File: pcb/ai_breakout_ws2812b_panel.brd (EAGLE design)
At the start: 92.2 x 100 mm, 280 parts

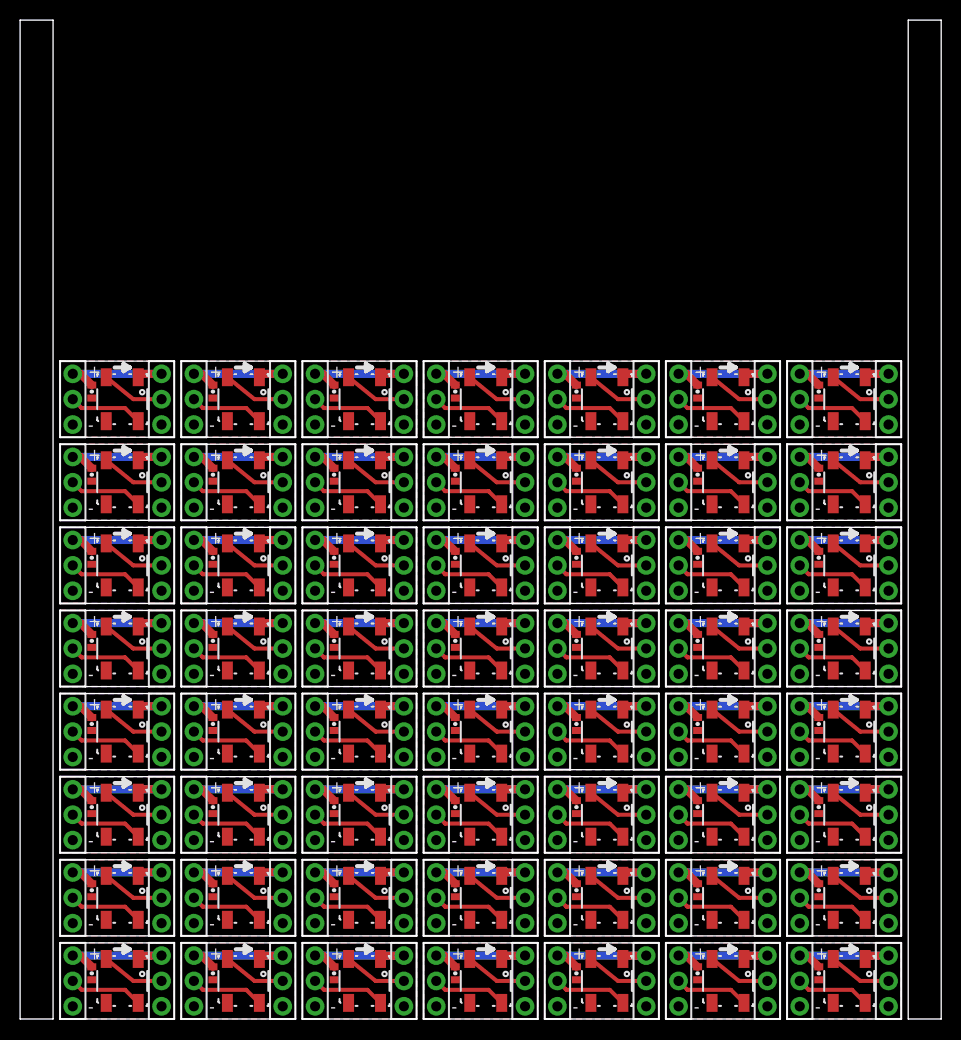
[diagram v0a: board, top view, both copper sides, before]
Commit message: adding panelized version
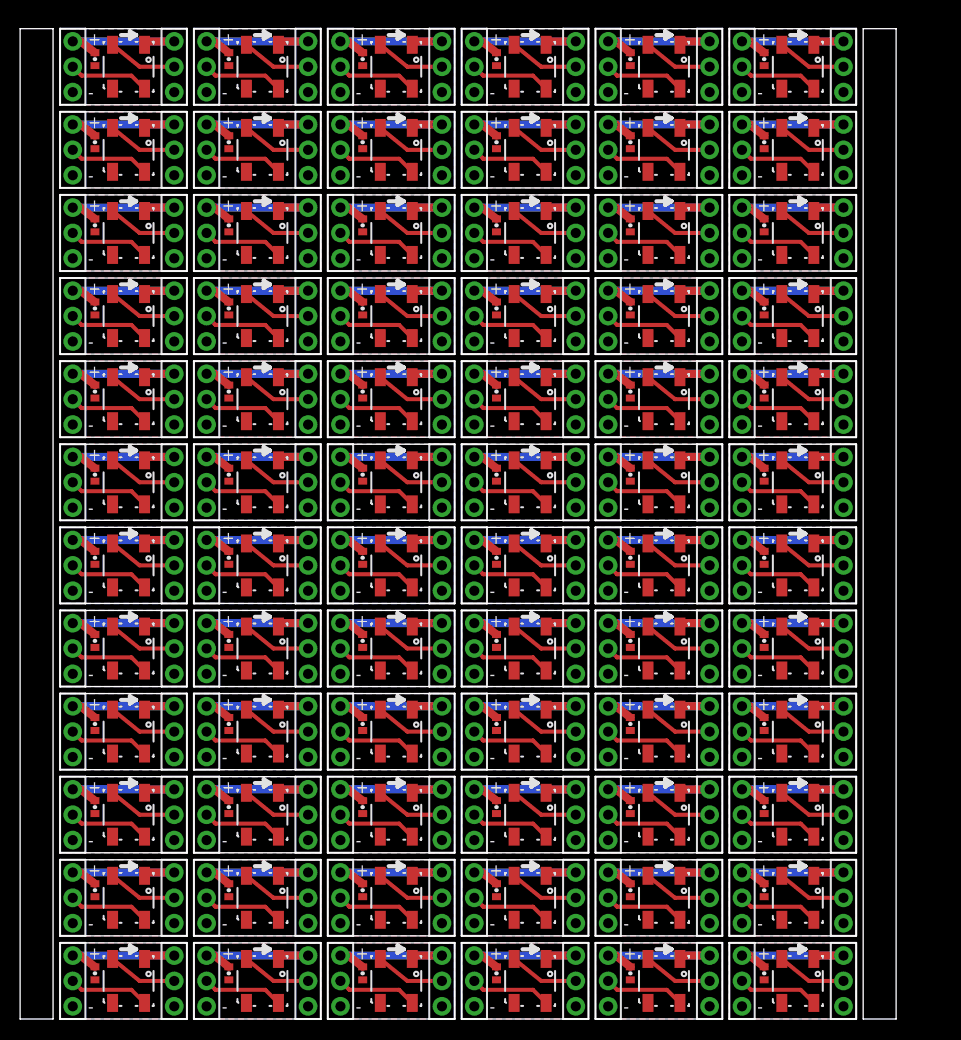
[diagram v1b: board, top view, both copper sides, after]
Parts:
- added C57, C58, C59, C60, C61, C62, C63, C64, C65, C66, C67, C68, C69, C70, C71, C72: 0.1uF, Ai_Passives:CAP-0402
- added IN56, IN57, IN58, IN59, IN60, IN61, IN62, IN63, IN64, IN65, IN66, IN67, IN68, IN69, IN70, IN71: 1X03, Ai_Connectors:1X03
- added OUT56, OUT57, OUT58, OUT59, OUT60, OUT61, OUT62, OUT63, OUT64, OUT65, OUT66, OUT67, OUT68, OUT69, OUT70, OUT71: 1X03NOFIRST, Ai_Connectors:1X03-NOFIRST
- added RGB56, RGB57, RGB58, RGB59, RGB60, RGB61, RGB62, RGB63, RGB64, RGB65, RGB66, RGB67, RGB68, RGB69, RGB70, RGB71: LED-WS2812B-SM, Ai_LED:LED-WS2812B-SM
- added U$57, U$58, U$59, U$60, U$61, U$62, U$63, U$64, U$65, U$66, U$67, U$68, U$69, U$70, U$71, U$72: (no value), Ai_Miscellany:AI-LOGO-XS
- moved IN32 70.0 mm to (32.1, 70.4)
- moved IN33 70.0 mm to (32.1, 78.7)
- moved IN34 70.0 mm to (32.1, 87.0)
- moved IN35 70.0 mm to (32.1, 95.3)
- moved C33 69.9 mm to (34.3, 71.1)
- moved C34 69.9 mm to (34.3, 79.5)
- moved C35 69.9 mm to (34.3, 87.8)
- moved C36 69.9 mm to (34.3, 96.1)
- moved RGB32 69.8 mm to (37.7, 70.4)
- moved RGB33 69.8 mm to (37.7, 78.7)
- moved RGB34 69.8 mm to (37.7, 87.0)
- moved RGB35 69.8 mm to (37.7, 95.3)
- moved U$33 69.7 mm to (38.4, 69.2)
- moved U$34 69.7 mm to (38.4, 77.5)
- moved U$35 69.7 mm to (38.4, 85.9)
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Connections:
- new net DI56: IN56.2, RGB56.4
- new net DI57: IN57.2, RGB57.4
- new net DI58: IN58.2, RGB58.4
- new net DI59: IN59.2, RGB59.4
- new net DI60: IN60.2, RGB60.4
- new net DI61: IN61.2, RGB61.4
- new net DI62: IN62.2, RGB62.4
- new net DI63: IN63.2, RGB63.4
- new net DI64: IN64.2, RGB64.4
- new net DI65: IN65.2, RGB65.4
- new net DI66: IN66.2, RGB66.4
- new net DI67: IN67.2, RGB67.4
- new net DI68: IN68.2, RGB68.4
- new net DI69: IN69.2, RGB69.4
- new net DI70: IN70.2, RGB70.4
- new net DI71: IN71.2, RGB71.4
- new net DO56: OUT56.2, RGB56.2
- new net DO57: OUT57.2, RGB57.2
- new net DO58: OUT58.2, RGB58.2
- new net DO59: OUT59.2, RGB59.2
- new net DO60: OUT60.2, RGB60.2
- new net DO61: OUT61.2, RGB61.2
- new net DO62: OUT62.2, RGB62.2
- new net DO63: OUT63.2, RGB63.2
- new net DO64: OUT64.2, RGB64.2
- new net DO65: OUT65.2, RGB65.2
- new net DO66: OUT66.2, RGB66.2
- new net DO67: OUT67.2, RGB67.2
- new net DO68: OUT68.2, RGB68.2
- new net DO69: OUT69.2, RGB69.2
- new net DO70: OUT70.2, RGB70.2
- new net DO71: OUT71.2, RGB71.2
- new net GND56: C57.2, IN56.1, OUT56.1, RGB56.3
- new net GND57: C58.2, IN57.1, OUT57.1, RGB57.3
- new net GND58: C59.2, IN58.1, OUT58.1, RGB58.3
- new net GND59: C60.2, IN59.1, OUT59.1, RGB59.3
- new net GND60: C61.2, IN60.1, OUT60.1, RGB60.3
- new net GND61: C62.2, IN61.1, OUT61.1, RGB61.3
- new net GND62: C63.2, IN62.1, OUT62.1, RGB62.3
- new net GND63: C64.2, IN63.1, OUT63.1, RGB63.3
- new net GND64: C65.2, IN64.1, OUT64.1, RGB64.3
- new net GND65: C66.2, IN65.1, OUT65.1, RGB65.3
- new net GND66: C67.2, IN66.1, OUT66.1, RGB66.3
- new net GND67: C68.2, IN67.1, OUT67.1, RGB67.3
- new net GND68: C69.2, IN68.1, OUT68.1, RGB68.3
- new net GND69: C70.2, IN69.1, OUT69.1, RGB69.3
- new net GND70: C71.2, IN70.1, OUT70.1, RGB70.3
- new net GND71: C72.2, IN71.1, OUT71.1, RGB71.3
- new net VCC56: C57.1, IN56.3, OUT56.3, RGB56.1
- new net VCC57: C58.1, IN57.3, OUT57.3, RGB57.1
- new net VCC58: C59.1, IN58.3, OUT58.3, RGB58.1
- new net VCC59: C60.1, IN59.3, OUT59.3, RGB59.1
- new net VCC60: C61.1, IN60.3, OUT60.3, RGB60.1
- new net VCC61: C62.1, IN61.3, OUT61.3, RGB61.1
- new net VCC62: C63.1, IN62.3, OUT62.3, RGB62.1
- new net VCC63: C64.1, IN63.3, OUT63.3, RGB63.1
- new net VCC64: C65.1, IN64.3, OUT64.3, RGB64.1
- new net VCC65: C66.1, IN65.3, OUT65.3, RGB65.1
- new net VCC66: C67.1, IN66.3, OUT66.3, RGB66.1
- new net VCC67: C68.1, IN67.3, OUT67.3, RGB67.1
- new net VCC68: C69.1, IN68.3, OUT68.3, RGB68.1
- new net VCC69: C70.1, IN69.3, OUT69.3, RGB69.1
- new net VCC70: C71.1, IN70.3, OUT70.3, RGB70.1
- new net VCC71: C72.1, IN71.3, OUT71.3, RGB71.1
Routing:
- net VCC71: track 0.00 -> 15.9 mm
- net VCC70: track 0.00 -> 15.9 mm
- net VCC69: track 0.00 -> 15.9 mm
- net VCC68: track 0.00 -> 15.9 mm
- net VCC67: track 0.00 -> 15.9 mm
- net VCC66: track 0.00 -> 15.9 mm
- net VCC65: track 0.00 -> 15.9 mm
- net VCC64: track 0.00 -> 15.9 mm
- net VCC63: track 0.00 -> 15.9 mm
- net VCC62: track 0.00 -> 15.9 mm
- net VCC61: track 0.00 -> 15.9 mm
- net VCC60: track 0.00 -> 15.9 mm
- net VCC59: track 0.00 -> 15.9 mm
- net VCC58: track 0.00 -> 15.9 mm
- net VCC57: track 0.00 -> 15.9 mm
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- added copper zone on layer 1, net GND56
- added copper zone on layer 16, net GND56
- added copper zone on layer 1, net GND57
- added copper zone on layer 16, net GND57
- added copper zone on layer 1, net GND58
- added copper zone on layer 16, net GND58
- added copper zone on layer 1, net GND59
- added copper zone on layer 16, net GND59
- added copper zone on layer 1, net GND60
- added copper zone on layer 16, net GND60
- added copper zone on layer 1, net GND61
- added copper zone on layer 16, net GND61
- added copper zone on layer 1, net GND62
- added copper zone on layer 16, net GND62
- added copper zone on layer 1, net GND63
- added copper zone on layer 16, net GND63
- added copper zone on layer 1, net GND64
- added copper zone on layer 16, net GND64
- added copper zone on layer 1, net GND65
- added copper zone on layer 16, net GND65
- added copper zone on layer 1, net GND66
- added copper zone on layer 16, net GND66
- added copper zone on layer 1, net GND67
- added copper zone on layer 16, net GND67
- added copper zone on layer 1, net GND68
- added copper zone on layer 16, net GND68
- added copper zone on layer 1, net GND69
- added copper zone on layer 16, net GND69
- added copper zone on layer 1, net GND70
- added copper zone on layer 16, net GND70
- added copper zone on layer 1, net GND71
- added copper zone on layer 16, net GND71
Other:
- board size 92.2 x 100 mm -> 87.7 x 99.1 mm
